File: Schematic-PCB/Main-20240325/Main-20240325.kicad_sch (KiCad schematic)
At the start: 16 parts, among them J1 Conn_01x20_Pin, J2 Conn_01x02_Pin, J3 Conn_01x03_Pin, J6 Conn_01x15_Pin, U1 DEV-16771, U4 MOUDLE-SEEEDUINO-XIAO-ESP32C3

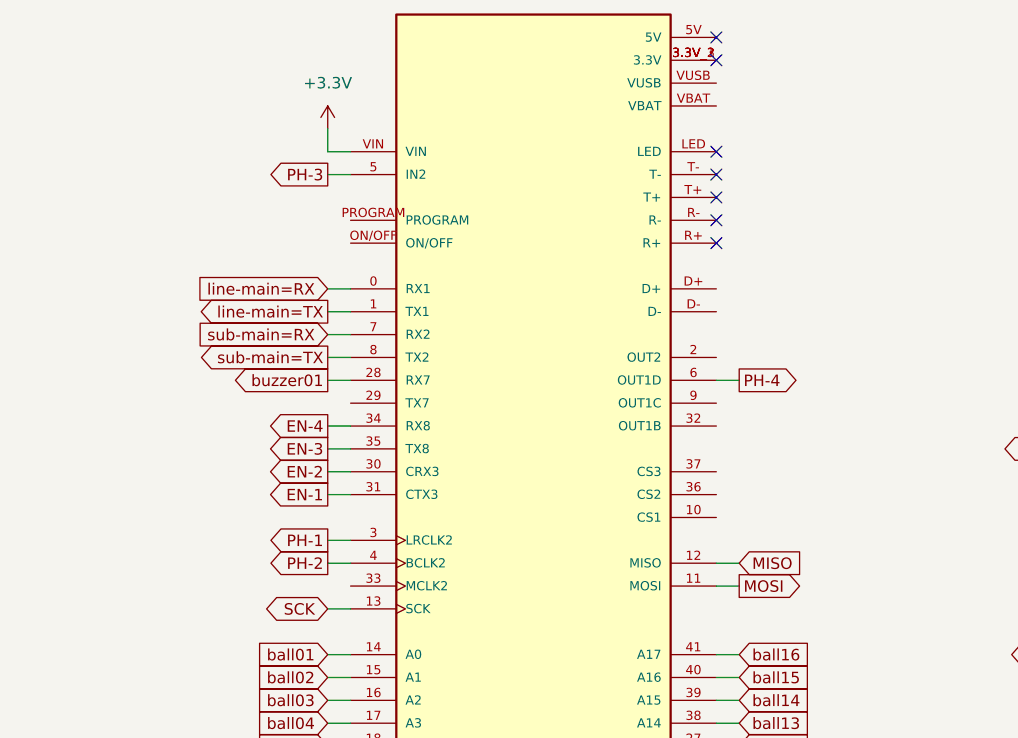
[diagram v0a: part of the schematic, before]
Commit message: メイン基板の回路図を再度更新
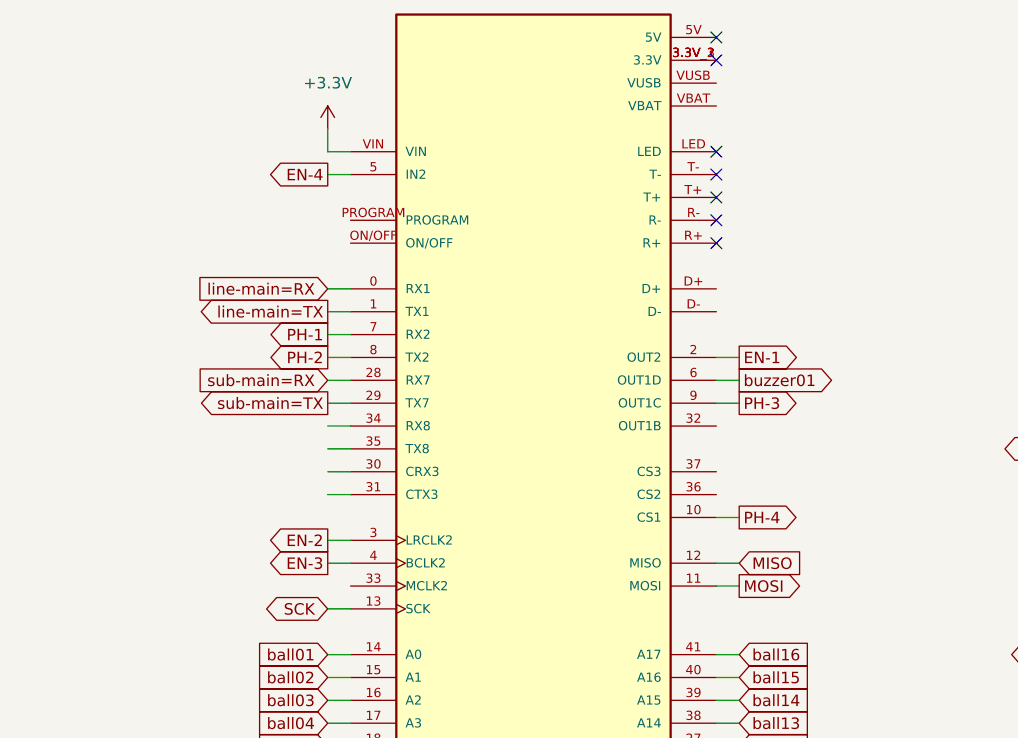
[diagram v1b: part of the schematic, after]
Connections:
- net EN-1: now also U1.2 (OUT2); no longer U1.31 (CTX3)
- net EN-2: now also U1.3 (LRCLK2); no longer U1.30 (CRX3)
- net EN-3: now also U1.4 (BCLK2); no longer U1.35 (TX8)
- net EN-4: now also U1.5 (IN2); no longer U1.34 (RX8)
- net PH-1: now also U1.7 (RX2); no longer U1.3 (LRCLK2)
- net PH-2: now also U1.8 (TX2); no longer U1.4 (BCLK2)
- net PH-3: now also U1.9 (OUT1C); no longer U1.5 (IN2)
- net PH-4: now also U1.10 (CS1); no longer U1.6 (OUT1D)
- net buzzer01: now also U1.6 (OUT1D); no longer U1.28 (RX7)
- net sub-main=RX: now also U1.28 (RX7); no longer U1.7 (RX2)
- net sub-main=TX: now also U1.29 (TX7); no longer U1.8 (TX2)

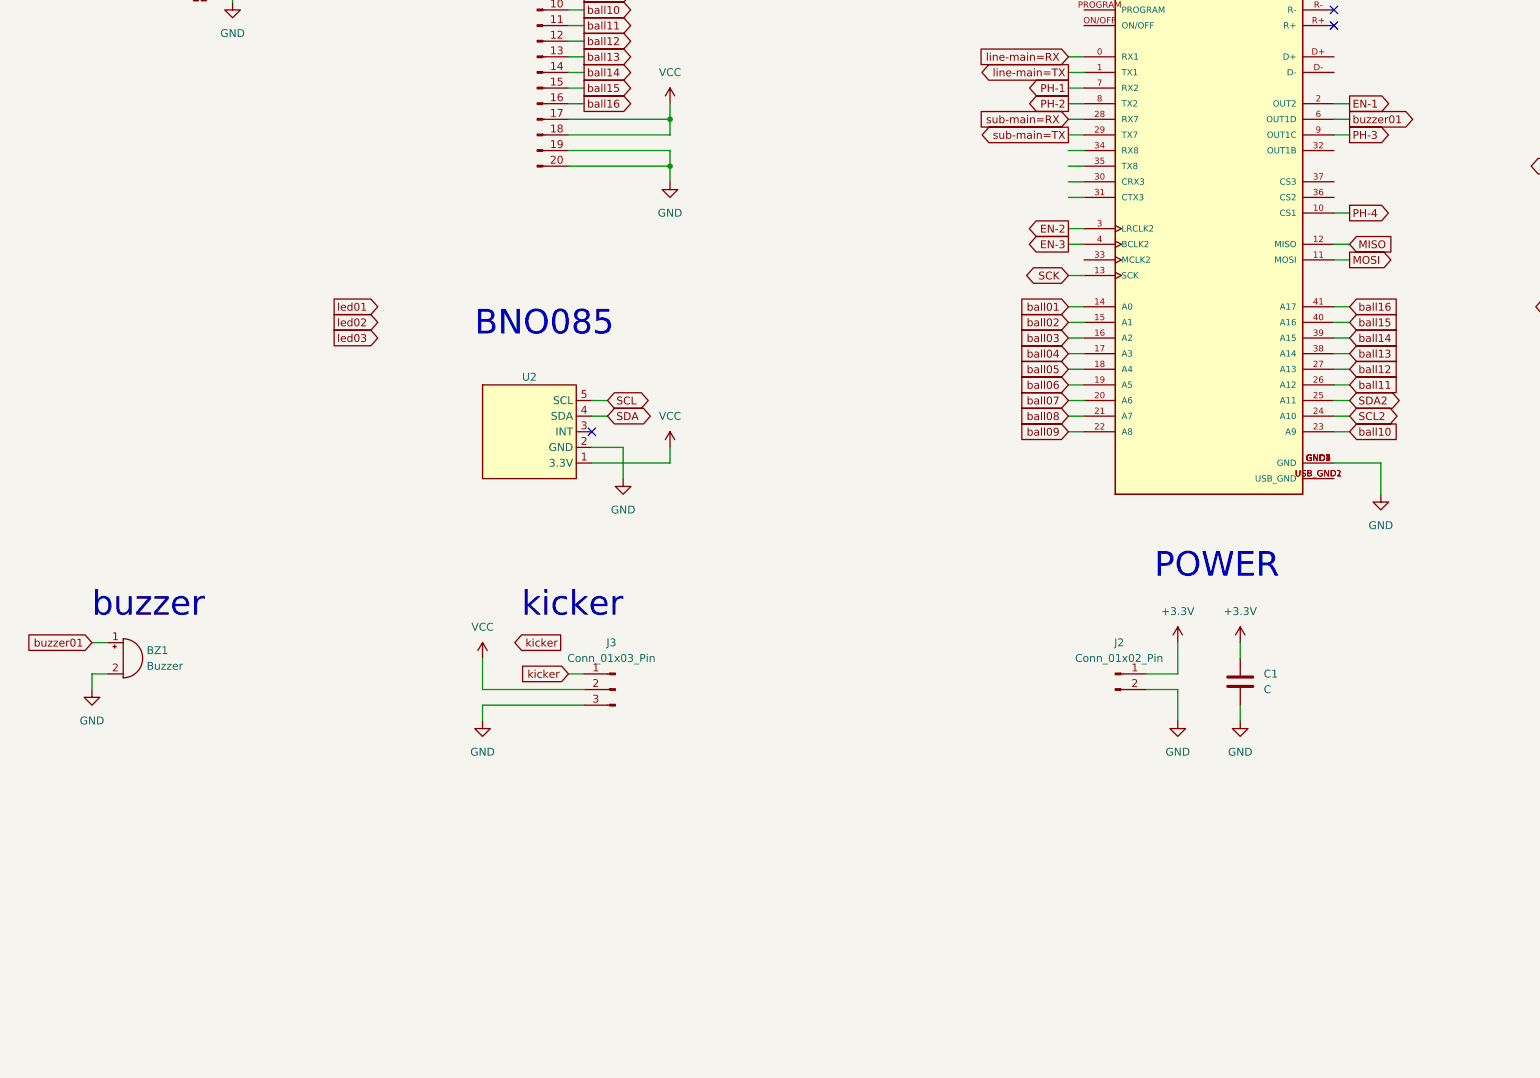
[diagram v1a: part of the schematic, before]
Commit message: メイン基板の回路図を更新
UI基板とのコネクタを作成・ピンを指定
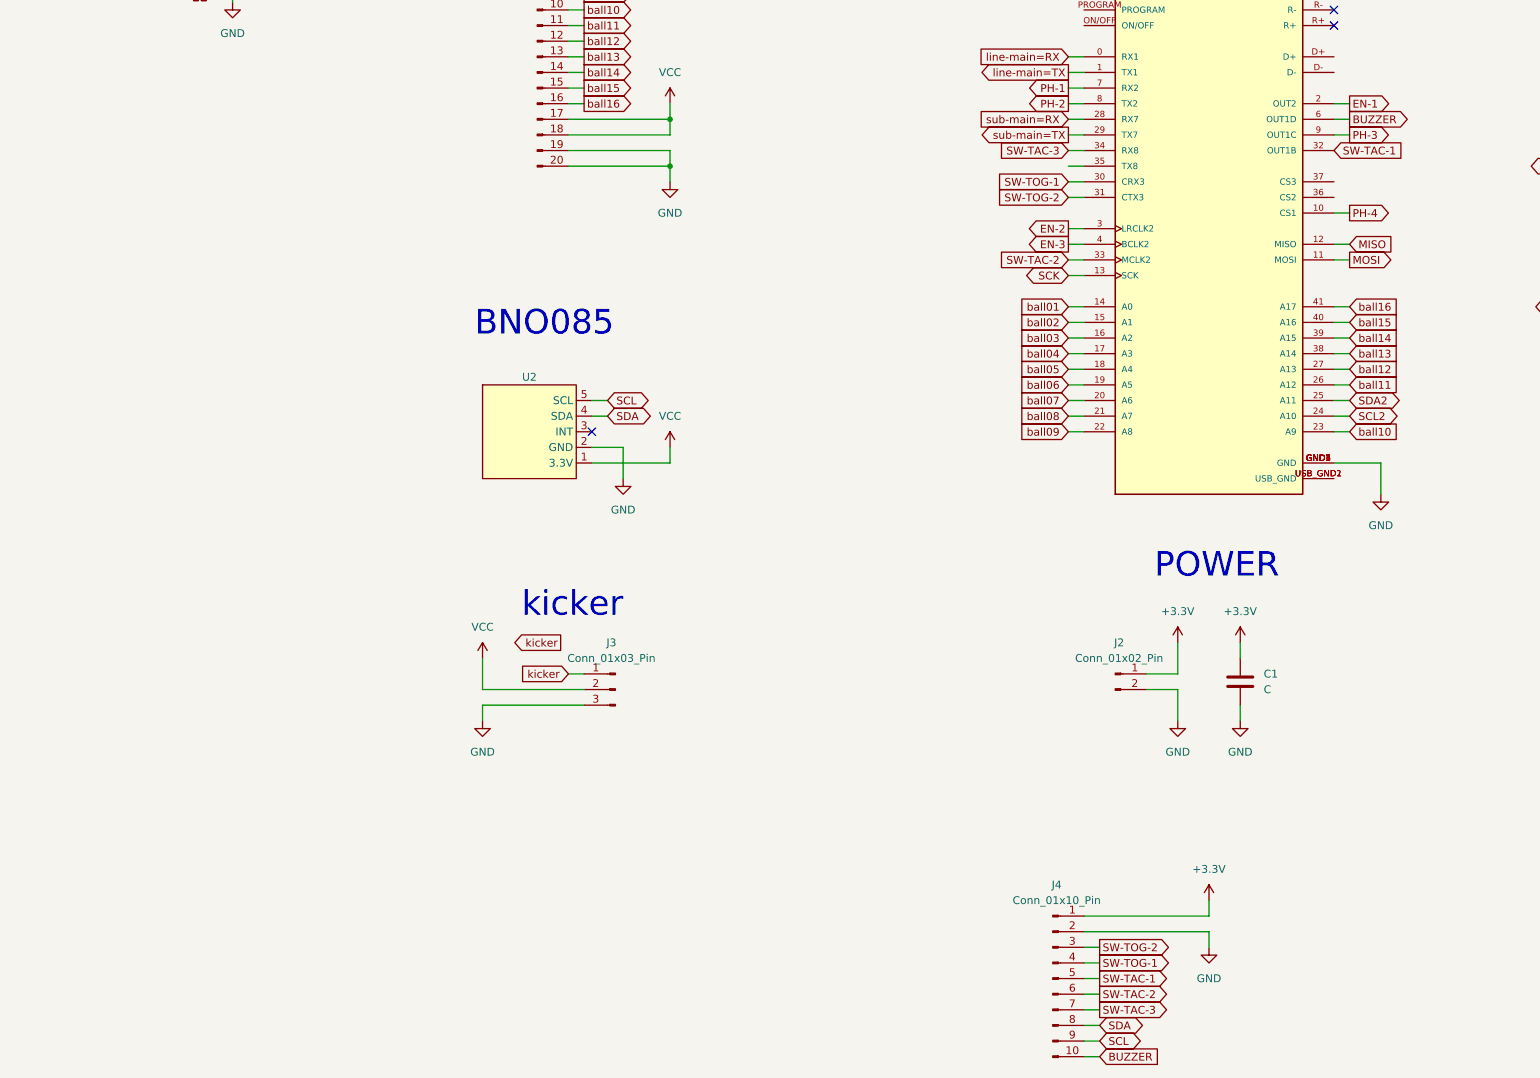
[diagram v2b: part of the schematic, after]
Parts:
- removed BZ1: Buzzer, symbol Device:Buzzer
- added J4: Conn_01x10_Pin, symbol Connector:Conn_01x10_Pin
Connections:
- net +3.3V: now also J4.1 (Pin_1)
- net GND: now also J4.2 (Pin_2)
- net SCL: now also J4.9 (Pin_9)
- net SDA: now also J4.8 (Pin_8)
- net SW-TOG-1: now reaches U1.30 (CRX3)
- net SW-TOG-1: now also J4.4 (Pin_4)
- net SW-TOG-2: now reaches U1.31 (CTX3)
- net SW-TOG-2: now also J4.3 (Pin_3)
- net SW-TAC-1: now reaches U1.32 (OUT1B)
- net SW-TAC-1: now also J4.5 (Pin_5)
- net SW-TAC-2: now reaches U1.33 (MCLK2)
- net SW-TAC-2: now also J4.6 (Pin_6)
- net SW-TAC-3: now reaches U1.34 (RX8)
- net SW-TAC-3: now also J4.7 (Pin_7)
- net buzzer01 renamed BUZZER
- net BUZZER: now also J4.10 (Pin_10)
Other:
- note removed: "buzzer"

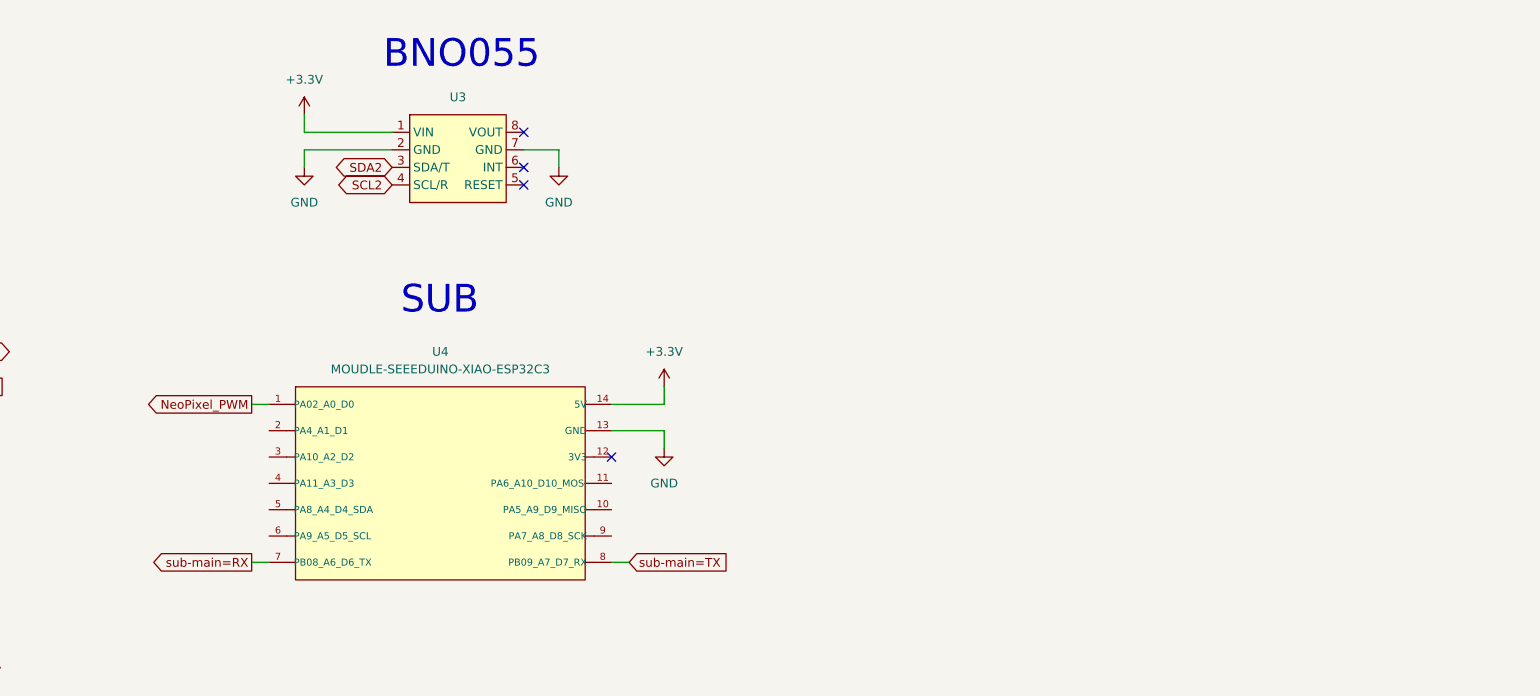
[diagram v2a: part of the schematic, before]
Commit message: 電源基板の回路図/PCBデザインを更新しました。
メイン基板への供給ラインを増やしました。
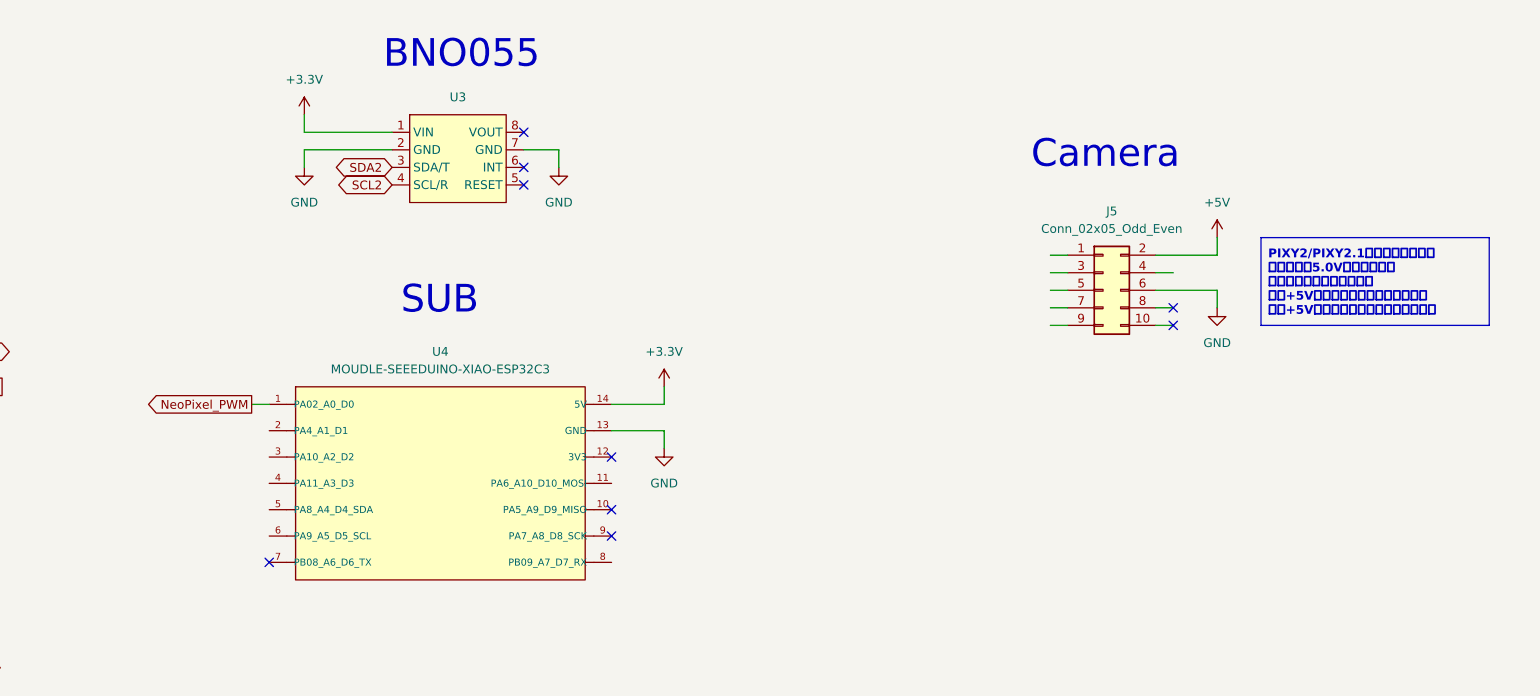
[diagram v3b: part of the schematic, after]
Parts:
- added J5: Conn_02x05_Odd_Even, symbol Connector_Generic:Conn_02x05_Odd_Even
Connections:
- net GND: now also J5.6 (Pin_6)
- net sub-main=RX: no longer U4.7 (PB08_A6_D6_TX)
- net sub-main=TX: no longer U4.8 (PB09_A7_D7_RX)
- new net +5V: J5.2 (Pin_2)
- no-connect marks 12 -> 17
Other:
- note added: "Camera"
